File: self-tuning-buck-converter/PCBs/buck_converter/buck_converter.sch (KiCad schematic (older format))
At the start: 48 parts, among them Q1 NMOS, U1 AMP from lab, U2 LM7322, U3 LT1999-50, U4 LD1117V50, U6 ESP32-DEVKITC-32D, U7 IR2125, U8 MAX11644

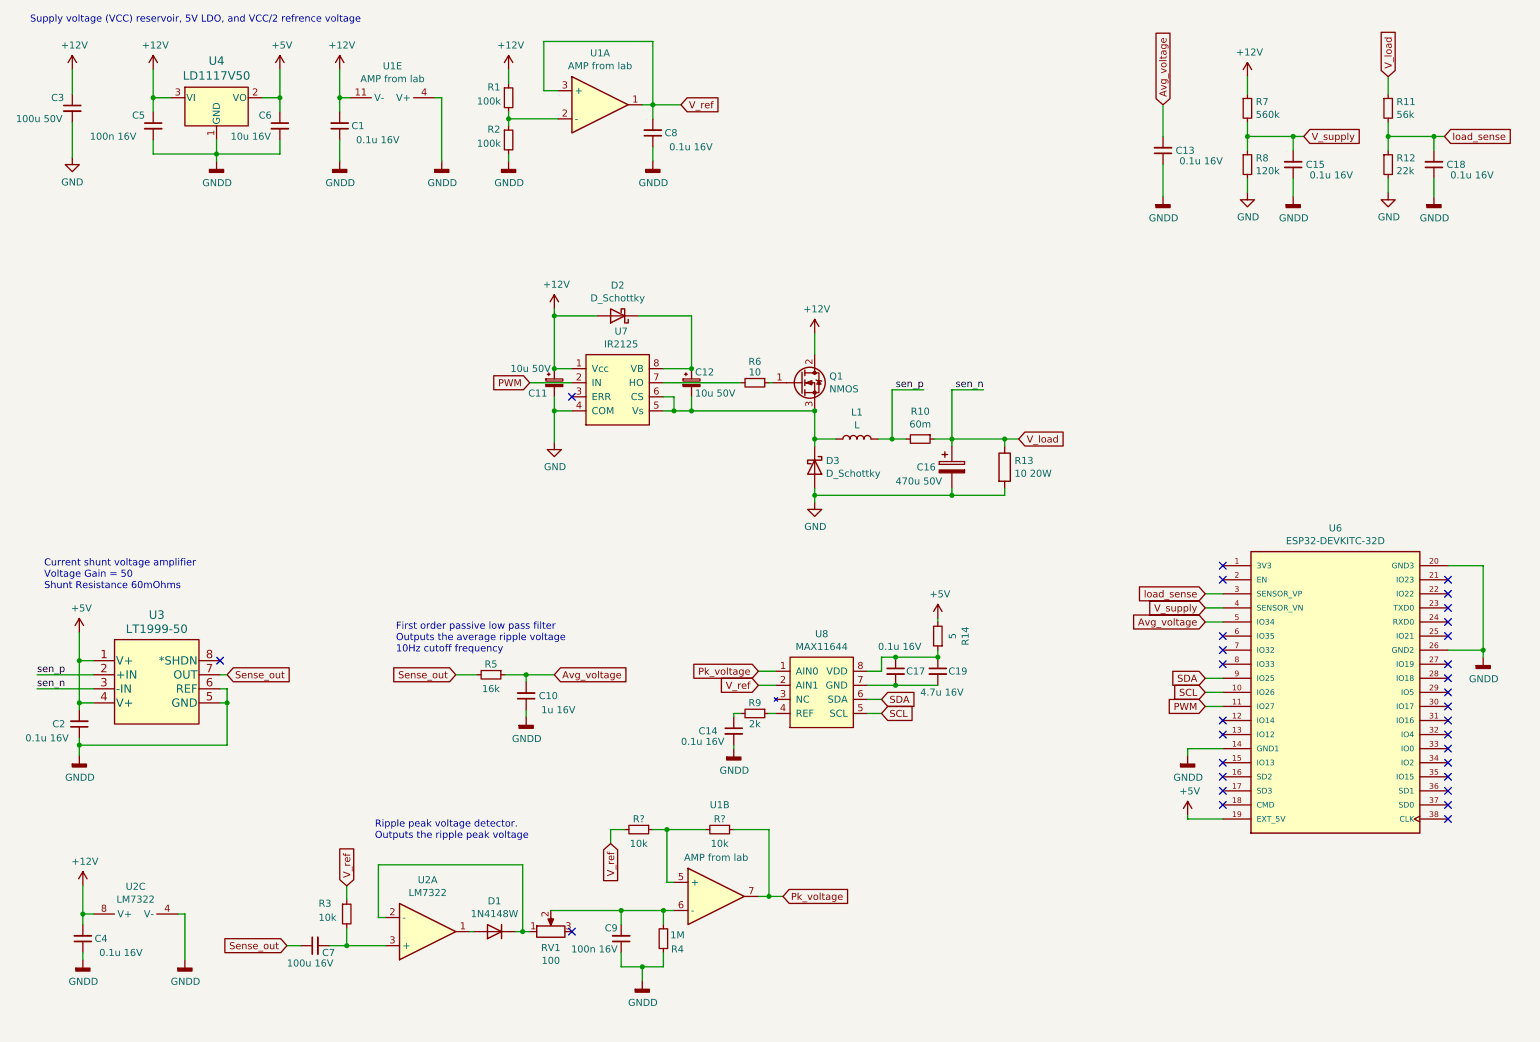
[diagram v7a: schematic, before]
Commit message: begin and almost complete the PCB design of the buck converter:
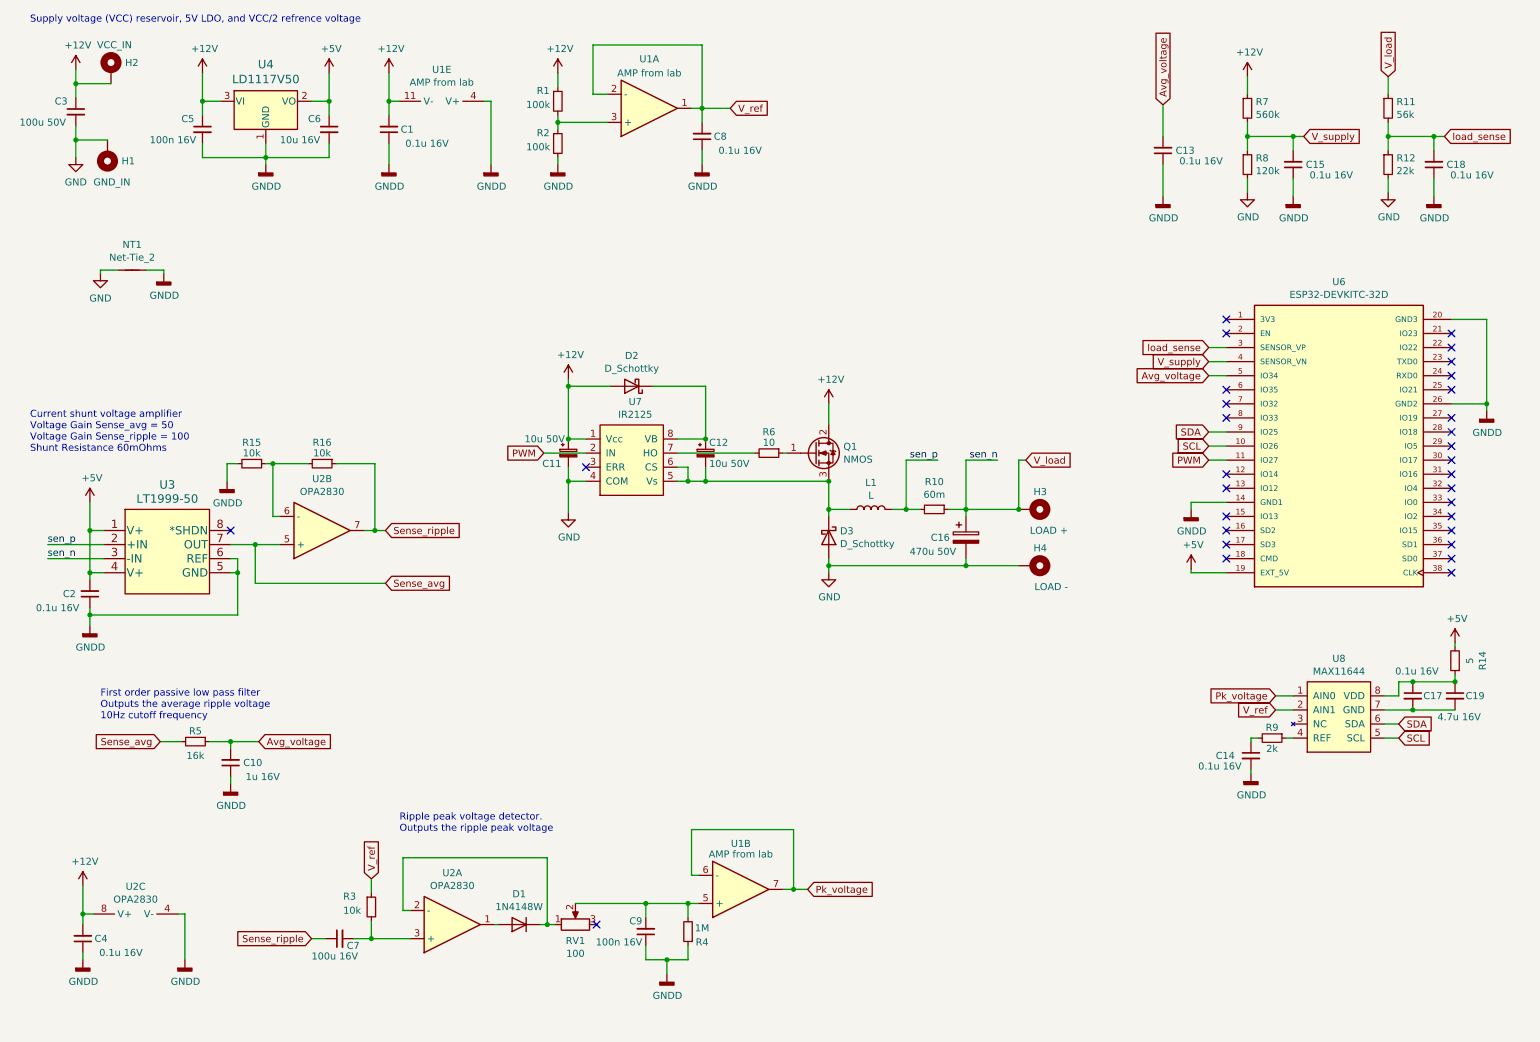
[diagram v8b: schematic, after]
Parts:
- removed R13: 10 20W, symbol Device:R
- removed R? (x2): 10k, Resistor_SMD:R_0603_1608Metric_Pad0.98x0.95mm_HandSolder, symbol Device:R_Small
- added H1: GND_IN, MountingHole:MountingHole_3.5mm_Pad_Via, symbol Mechanical:MountingHole_Pad
- added H2: VCC_IN, MountingHole:MountingHole_3.5mm_Pad_Via, symbol Mechanical:MountingHole_Pad
- added H3: LOAD +, MountingHole:MountingHole_3.5mm_Pad_Via, symbol Mechanical:MountingHole_Pad
- added H4: LOAD -, MountingHole:MountingHole_3.5mm_Pad_Via, symbol Mechanical:MountingHole_Pad
- added NT1: Net-Tie_2, NetTie:NetTie-2_SMD_Pad2.0mm, symbol Device:Net-Tie_2
- added R15, R16: 10k, Resistor_SMD:R_0603_1608Metric_Pad1.05x0.95mm_HandSolder, symbol Device:R_Small
- added unit 2 of U2
- C16: footprint (none) -> multi_capacitor:multi_cap
- L1: footprint (none) -> IND_HCTI-150-5.0:IND_HCTI-150-5.0
- R10: footprint (none) -> Resistor_SMD:R_2512_6332Metric_Pad1.52x3.35mm_HandSolder
- U2: value LM7322 -> OPA2830
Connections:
- net +12V: now also H2.1
- net GND: now also H1.1, H4.1, NT1.1
- net GNDD: now also NT1.2, R15.2
- net Pk_voltage: now also U1.6 (-)
- net V_load: now also H3.1
- net V_ref: now also U1.2 (-); no longer U1.3 (+)
- net at R1.2, R2.1: now also U1.3 (+); no longer U1.2 (-)
- net at C9.2, R4.2, RV1.2: now also U1.5 (+); no longer U1.6 (-)
- net Sense_out renamed Sense_avg
- net Sense_avg: now also U2.5 (+); no longer C7.1
- new net: R15.1, R16.2, U2.6 (-)
- new net Sense_ripple: C7.1, R16.1, U2.7
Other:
- note added: "Current shunt voltage amplifier\nVoltage Gain Sense_avg = 50\nVoltage Gain Sense_ripple = 100\nShunt Resistance 60mOhms\n"
- note removed: "Current shunt voltage amplifier\nVoltage Gain = 50\nShunt Resistance 60mOhms"
- moved on the sheet: C1, C10, C11, C12, C14, C16, C17, C19, C2, C3, C5, C6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
